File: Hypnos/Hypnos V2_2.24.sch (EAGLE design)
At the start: 32 parts

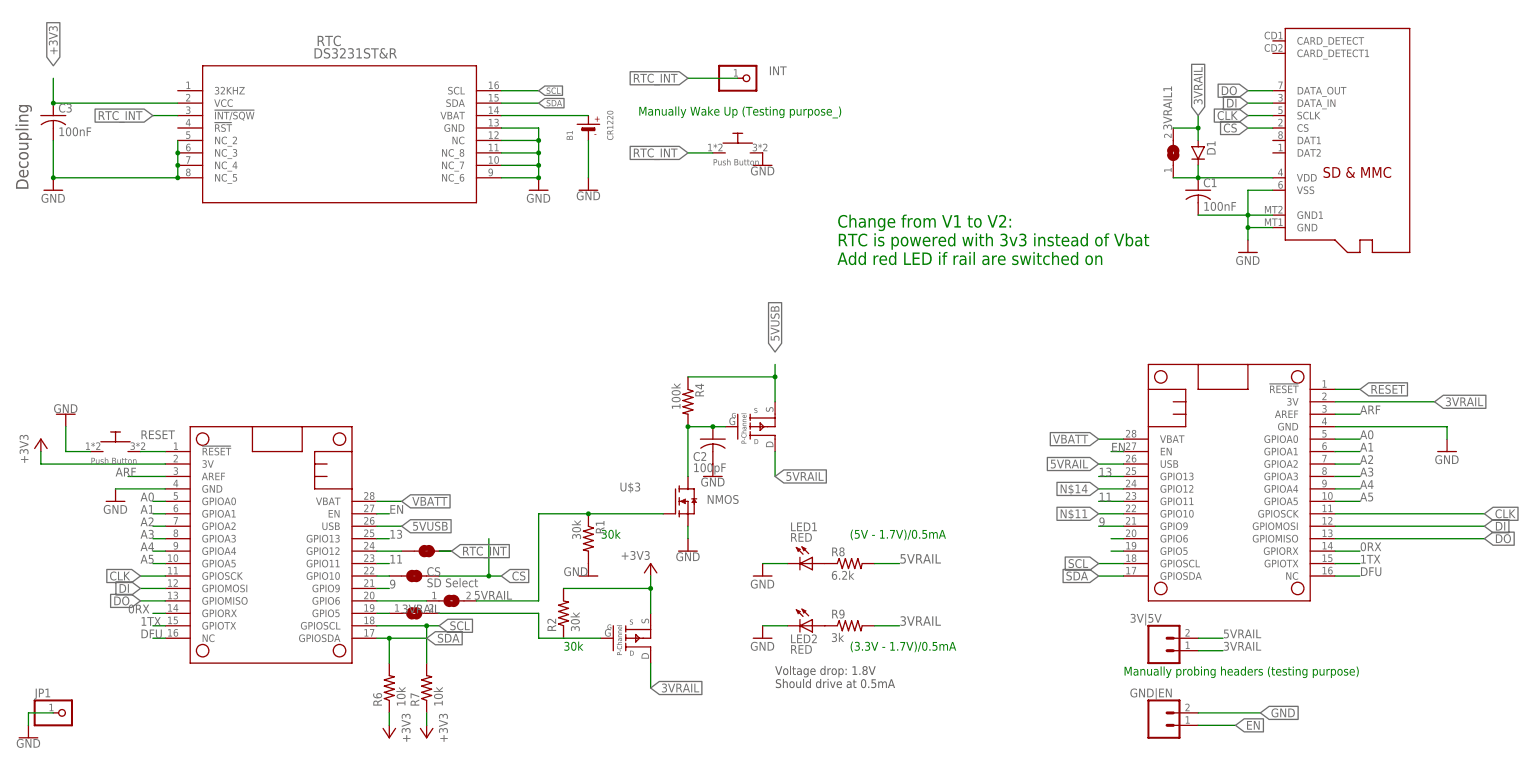
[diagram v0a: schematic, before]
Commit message: I2C line connected to 3.3Rail
Remoce I2C line from 3.3Rail reduce power going back to sersor when they are turned off.
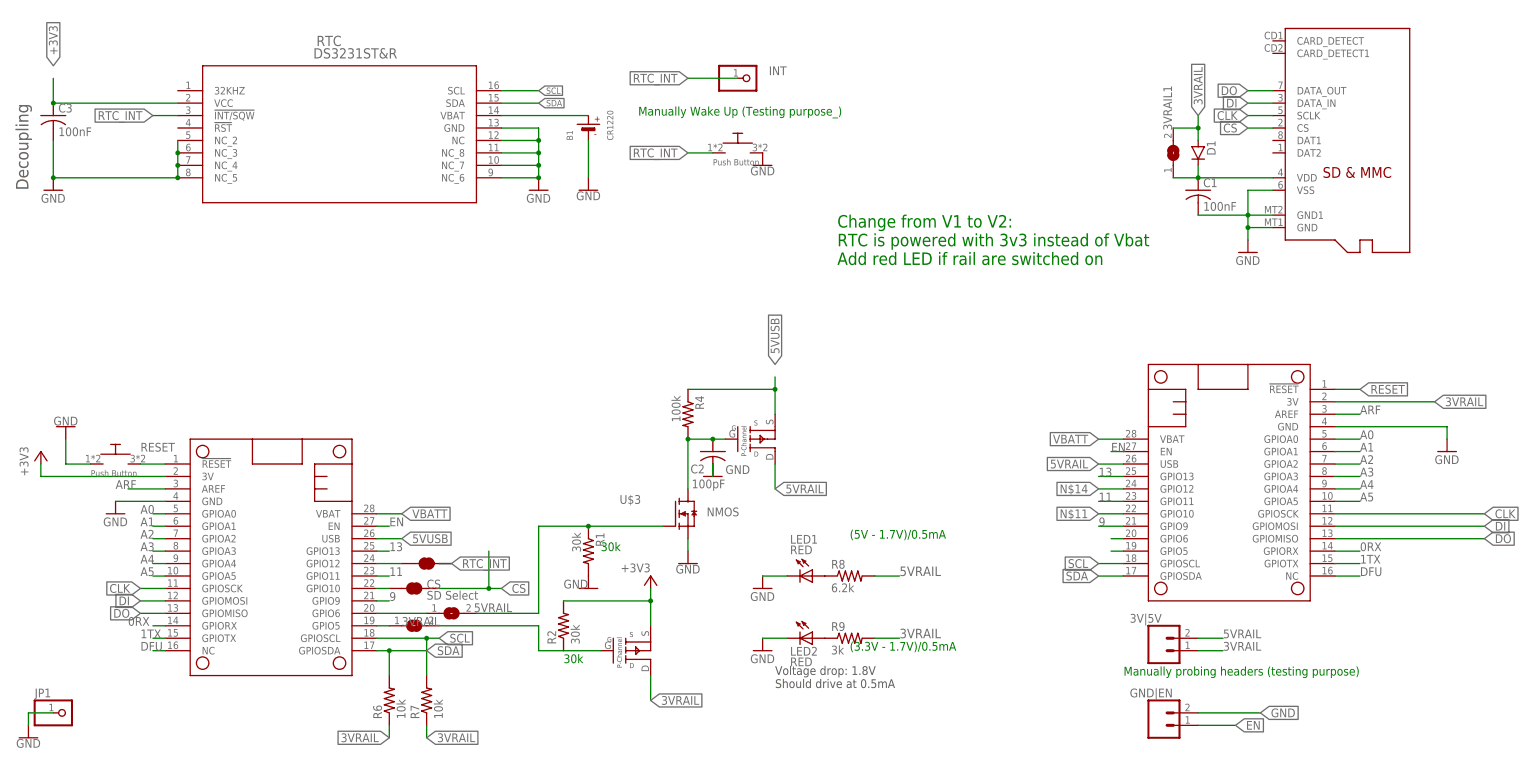
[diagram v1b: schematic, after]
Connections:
- net +3V3: no longer R6.1, R7.1
- net 3VRAIL: now also R6.1, R7.1
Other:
- moved on the sheet: 3VRAIL, 5VRAIL, C2, CS, LED1, LED2, R1, R2, R4, R6, R7, R8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
